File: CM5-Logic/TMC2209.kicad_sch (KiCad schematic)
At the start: 3 parts, among them J16 6130XX11821_61300811821, J17 6130XX11821_61300811821

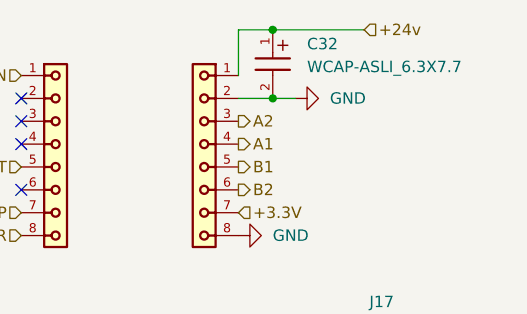
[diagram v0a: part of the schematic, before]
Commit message: adds a 24Pin ATX PSU interface for power and cleans up the amplifier hierarchy
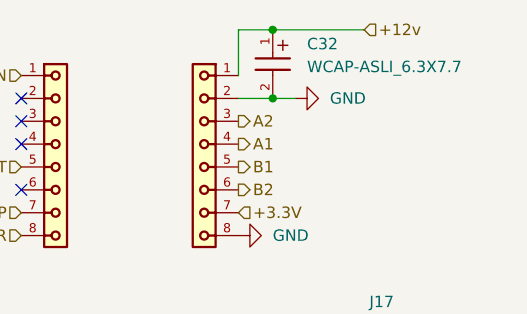
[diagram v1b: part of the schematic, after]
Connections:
- net +24v renamed +12v
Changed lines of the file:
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@@
 		)
 	)
-	(hierarchical_label "+24v"
+	(hierarchical_label "+12v"
 		(shape input)
 		(at 149.86 64.77 0)

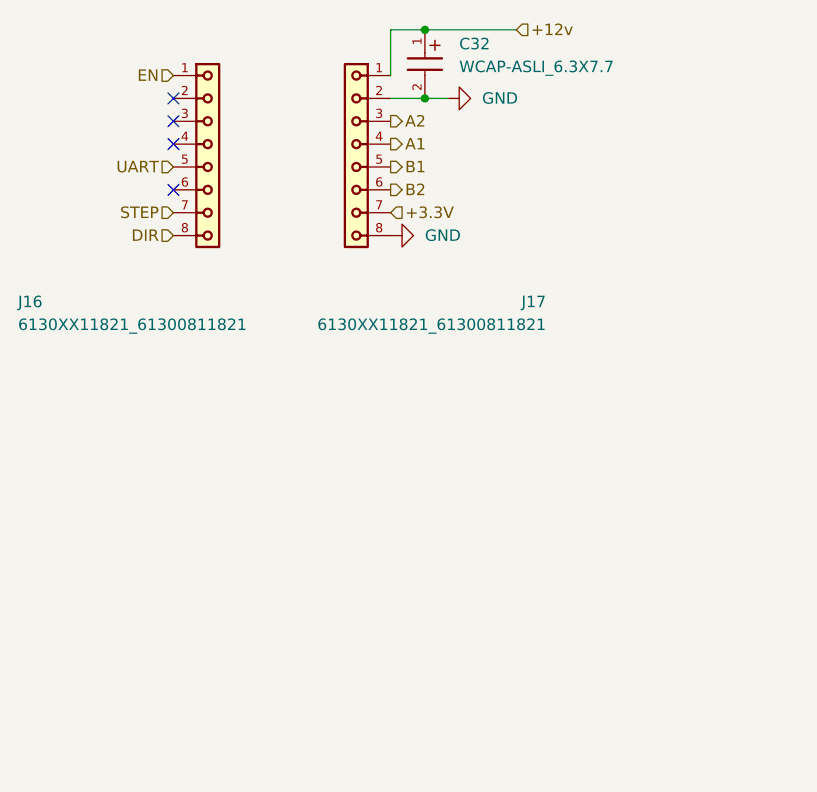
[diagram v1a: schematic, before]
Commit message: changes USB port, adds TMC2209 SilentStepStick footprint, redoes PCB Layout
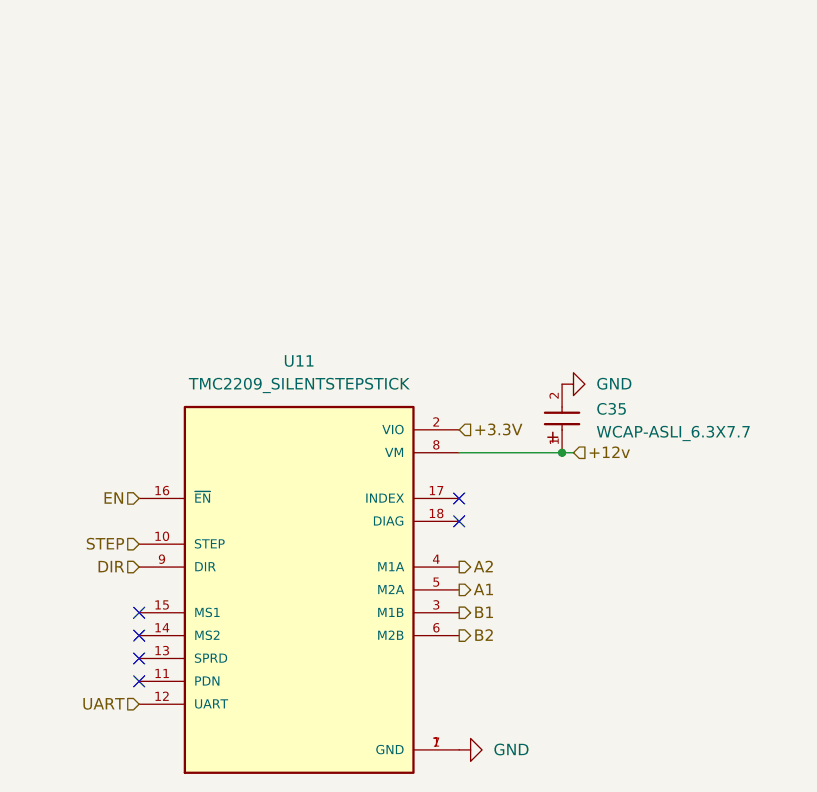
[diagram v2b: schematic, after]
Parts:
- removed C32: WCAP-ASLI_6.3X7.7, WCAP-ASLI_6.3X7.7:WCAP-ASLI_6.3X7.7_DXL_, symbol WCAP-ASLI_6.3X7.7:WCAP-ASLI_6.3X7.7
- removed J16, J17: 6130XX11821_61300811821, 6130XX11821_61300811821:61300811821, symbol 6130XX11821_61300811821:6130XX11821_61300811821
- added C35: WCAP-ASLI_6.3X7.7, Custom Components:WCAP-ASLI_6.3X7.7_DXL_, symbol WCAP-ASLI_6.3X7.7:WCAP-ASLI_6.3X7.7
- added U11: TMC2209_SILENTSTEPSTICK, TMC2209_SILENTSTEPSTICK:MODULE_TMC2209_SILENTSTEPSTICK, symbol TMC2209_SILENTSTEPSTICK:TMC2209_SILENTSTEPSTICK
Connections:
- net +12v: now also C35.1, U11.8 (VM)
- net +3.3V: now also U11.2 (VIO)
- net A1: now also U11.5 (M2A)
- net A2: now also U11.4 (M1A)
- net B1: now also U11.3 (M1B)
- net B2: now also U11.6 (M2B)
- net DIR: now also U11.9 (DIR)
- net EN: now also U11.16 (~{EN})
- net GND: now also C35.2, U11.1 (GND), U11.7 (GND)
- net STEP: now also U11.10 (STEP)
- net UART: now also U11.12 (UART)
- no-connect marks 4 -> 6

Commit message: Finishes PCB Pad Layout, Updates LED Status Circuit to RPI Foundations newest version
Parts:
- U11: footprint TMC2209_SILENTSTEPSTICK:MODULE_TMC2209_SILENTSTEPSTICK -> Custom Components:MODULE_TMC2209_SILENTSTEPSTICK
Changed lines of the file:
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@@
 			)
 		)
-		(property "Footprint" "TMC2209_SILENTSTEPSTICK:MODULE_TMC2209_SILENTSTEPSTICK"
+		(property "Footprint" "Custom Components:MODULE_TMC2209_SILENTSTEPSTICK"
 			(at 125.73 127 0)
 			(effects
